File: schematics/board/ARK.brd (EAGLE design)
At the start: 89.6 x 89 mm, 207 parts, among them IC2 STM32F103C8T, Q5 8MHz

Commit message: Изменения в компоновке БКУ
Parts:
- removed R25, R26: 10k, resistor:R0603
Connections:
- removed net N$156: IC2.38, R25.2
- removed net N$157: IC2.39, R26.2
- net VDD: no longer R25.1, R26.1
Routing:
- net N$156: track 4.93 -> 0.00 mm
- net N$157: track 4.22 -> 0.00 mm
- net VDD: track 279.9 -> 279.4 mm
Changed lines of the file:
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@@
 <attribute name="VALUE" x="62.53" y="20.945" size="1.27" layer="27"/>
 </element>
-<element name="R25" library="resistor" library_urn="urn:adsk.eagle:library:348" package="R0603" package3d_urn="urn:adsk.eagle:package:23555/3" value="10k" x="61.1" y="25.78" smashed="yes" rot="R90"/>
-<element name="R26" library="resistor" library_urn="urn:adsk.eagle:library:348" package="R0603" package3d_urn="urn:adsk.eagle:package:23555/3" value="10k" x="63.3" y="25.78" smashed="yes" rot="R90"/>
 <element name="R27" library="resistor" library_urn="urn:adsk.eagle:library:348" package="R0603" package3d_urn="urn:adsk.eagle:package:23555/3" value="10k" x="58.9" y="25.78" smashed="yes" rot="R90"/>
 <element name="R64" library="resistor" library_urn="urn:adsk.eagle:library:348" package="R0603" package3d_urn="urn:adsk.eagle:package:23555/3" value="10k" x="56.7" y="25.78" smashed="yes" rot="R90"/>
@@
 <contactref element="AB2" pad="3"/>
 <contactref element="AB1" pad="3"/>
-<contactref element="R25" pad="1"/>
-<contactref element="R26" pad="1"/>
 <contactref element="R27" pad="1"/>
 <contactref element="R64" pad="1"/>
@@
 <wire x1="56.7" y1="24.93" x2="57.85" y2="24.93" width="0.3" layer="1"/>
 <wire x1="57.85" y1="24.93" x2="58.9" y2="24.93" width="0.3" layer="1"/>
-<wire x1="61.1" y1="24.93" x2="58.9" y2="24.93" width="0.3" layer="1"/>
-<wire x1="61.1" y1="24.93" x2="63.3" y2="24.93" width="0.3" layer="1"/>
-<wire x1="63.3" y1="24.93" x2="63.05" y2="24.68" width="0.3" layer="1"/>
-<wire x1="63.05" y1="24.68" x2="63.05" y2="22.85" width="0.3" layer="1"/>
+<wire x1="63.05" y1="22.85" x2="63.05" y2="24.68" width="0.3" layer="1"/>
 <wire x1="63.05" y1="22.85" x2="63.05" y2="22.1" width="0.3" layer="1"/>
 <wire x1="63.05" y1="22.1" x2="63.05" y2="21.3" width="0.3" layer="1"/>
@@
 <wire x1="61.75" y1="39.55" x2="62.27478125" y2="39.02521875" width="0.25" layer="1"/>
 <wire x1="62.27478125" y1="39.02521875" x2="62.5206375" y2="39.02521875" width="0.25" layer="1"/>
+<wire x1="63.05" y1="24.68" x2="62.8" y2="24.93" width="0.3" layer="1"/>
+<wire x1="62.8" y1="24.93" x2="58.9" y2="24.93" width="0.3" layer="1"/>
 </signal>
 <signal name="GND">
@@
 <wire x1="73.05" y1="27.8" x2="74.55" y2="27.8" width="0.3" layer="1"/>
 </signal>
-<signal name="N$156">
-<contactref element="R25" pad="2"/>
-<wire x1="61.1" y1="26.63" x2="63.05" y2="28.58" width="0.3" layer="1"/>
-<wire x1="63.05" y1="28.58" x2="63.05" y2="30.75" width="0.3" layer="1"/>
-<contactref element="IC2" pad="38"/>
-</signal>
-<signal name="N$157">
-<contactref element="R26" pad="2"/>
-<wire x1="63.3" y1="26.63" x2="63.55" y2="26.88" width="0.3" layer="1"/>
-<wire x1="63.55" y1="30.75" x2="63.55" y2="26.88" width="0.3" layer="1"/>
-<contactref element="IC2" pad="39"/>
-</signal>
 <signal name="N$159">

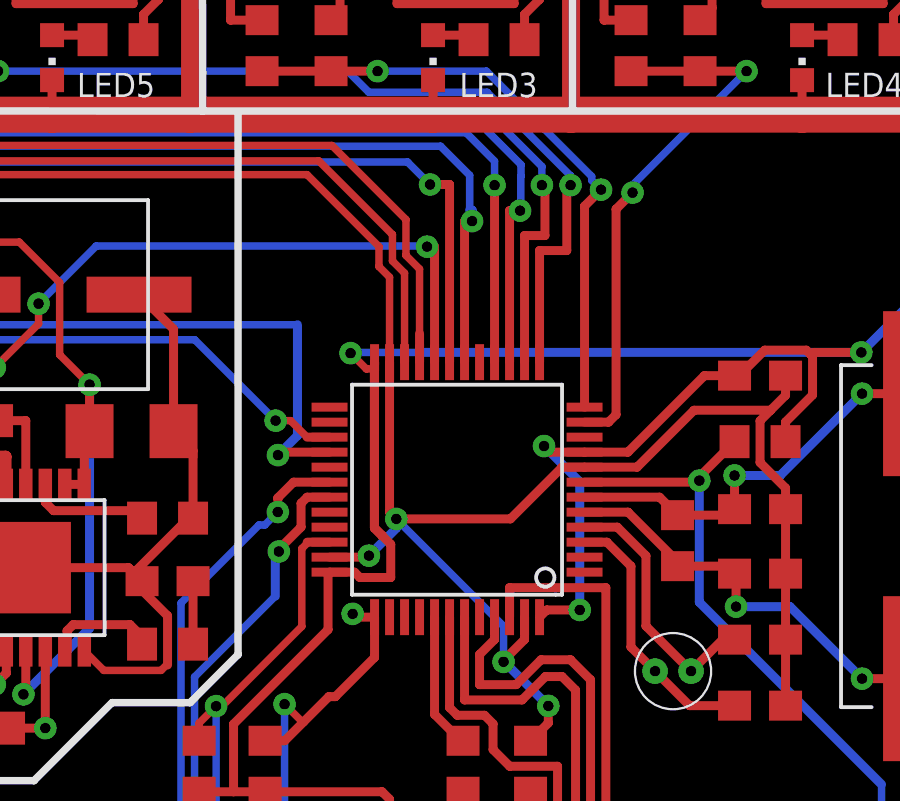
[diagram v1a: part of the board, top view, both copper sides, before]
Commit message: Исправлены АРК и БСК1
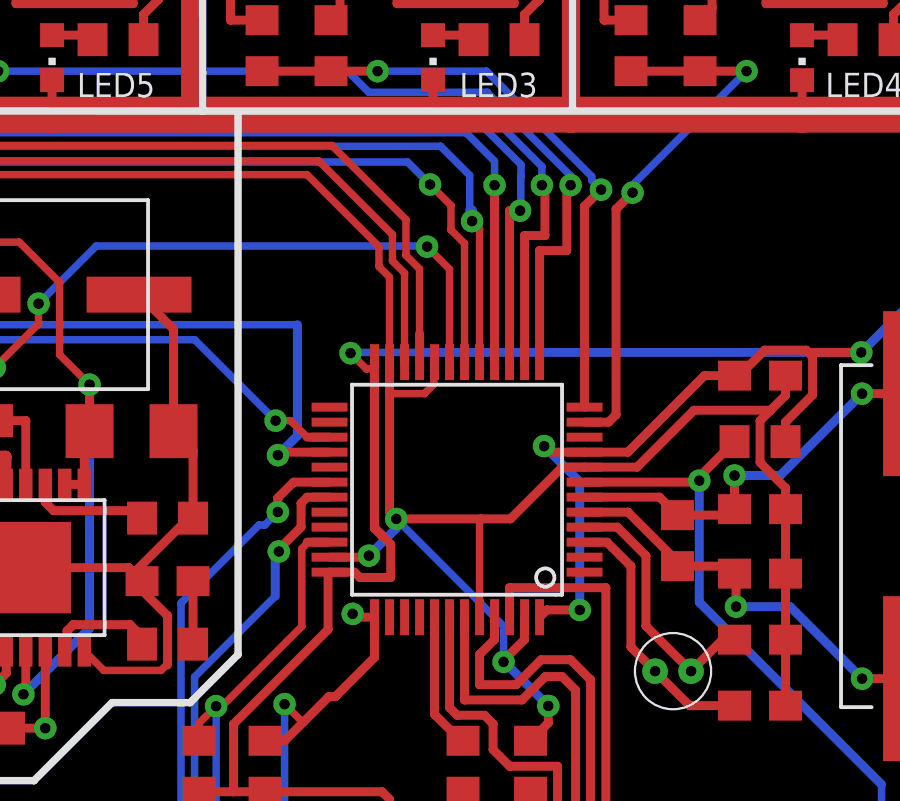
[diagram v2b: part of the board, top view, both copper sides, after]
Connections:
- net 1W: now also IC2.17; no longer IC2.18
- net GND: now also IC2.20, IC2.44
- net PGOOD1: now also IC2.18; no longer IC2.19
- net PGOOD2: now also IC2.19; no longer IC2.20
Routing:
- net GND: track 569.3 -> 574.9 mm
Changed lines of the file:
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@@
 <?xml version="1.0" encoding="utf-8"?>
 <!DOCTYPE eagle SYSTEM "eagle.dtd">
-<eagle version="9.6.0">
+<eagle version="9.4.2">
 <drawing>
 <settings>
@@
 <wire x1="63.05" y1="34.24983125" x2="63.274915625" y2="34.024915625" width="0.3" layer="1"/>
 <wire x1="69.55" y1="35.75" x2="68.805025" y2="35.75" width="0.3" layer="1"/>
-<wire x1="67.079940625" y1="34.024915625" x2="63.274915625" y2="34.024915625" width="0.3" layer="1"/>
+<wire x1="67.079940625" y1="34.024915625" x2="66.1" y2="34.024915625" width="0.3" layer="1"/>
+<wire x1="66.1" y1="34.024915625" x2="63.274915625" y2="34.024915625" width="0.3" layer="1"/>
 <wire x1="68.805025" y1="35.75" x2="67.079940625" y2="34.024915625" width="0.3" layer="1"/>
 <wire x1="51.55" y1="13.5" x2="52" y2="13.95" width="0.3" layer="1"/>
@@
 <wire x1="66.85" y1="29.26" x2="66.85" y2="29.305025" width="0.3" layer="1"/>
 <wire x1="66.85" y1="29.305025" x2="67.55" y2="30.005025" width="0.3" layer="1"/>
-<wire x1="63.05" y1="39.25" x2="63.05" y2="34.24983125" width="0.3" layer="1"/>
+<wire x1="63.05" y1="39.25" x2="63.05" y2="38.2" width="0.3" layer="1"/>
 <contactref element="R70" pad="1"/>
 <contactref element="R30" pad="2"/>
+<wire x1="63.05" y1="38.2" x2="63.05" y2="34.24983125" width="0.3" layer="1"/>
 <wire x1="46.4532" y1="36.35" x2="46.4532" y2="37.5968" width="0.3" layer="1"/>
 <wire x1="46.4532" y1="37.5968" x2="45.85" y2="38.2" width="0.3" layer="1"/>
@@
 <wire x1="63.274915625" y1="34.024915625" x2="66.85" y2="30.44983125" width="0.25" layer="16"/>
 <wire x1="66.85" y1="30.44983125" x2="66.85" y2="29.26" width="0.25" layer="16"/>
+<contactref element="IC2" pad="44"/>
+<contactref element="IC2" pad="20"/>
+<wire x1="64.55" y1="39.25" x2="64.525" y2="39.225" width="0.25" layer="1"/>
+<wire x1="64.525" y1="39.225" x2="64.525" y2="38.51538125" width="0.25" layer="1"/>
+<wire x1="64.525" y1="38.51538125" x2="64.20961875" y2="38.2" width="0.25" layer="1"/>
+<wire x1="64.20961875" y1="38.2" x2="63.05" y2="38.2" width="0.25" layer="1"/>
+<wire x1="66.05" y1="30.75" x2="66.05" y2="33.974915625" width="0.25" layer="1"/>
+<wire x1="66.05" y1="33.974915625" x2="66.1" y2="34.024915625" width="0.25" layer="1"/>
 </signal>
 <signal name="N$131">
@@
 <wire x1="20.72" y1="77.95" x2="20.72" y2="73.85" width="0.3" layer="16"/>
 <wire x1="20.72" y1="73.85" x2="20.77" y2="73.8" width="0.3" layer="16"/>
-<wire x1="65.55" y1="39.25" x2="65.55" y2="43.95" width="0.3" layer="1"/>
-<wire x1="65.55" y1="43.95" x2="65.8" y2="43.95" width="0.3" layer="1"/>
 <via x="65.8" y="43.95" extent="1-16" drill="0.35"/>
 <wire x1="65.8" y1="43.95" x2="65.8" y2="44.3202" width="0.3" layer="16"/>
@@
 <wire x1="12.8404" y1="47.1" x2="39.3702" y2="47.1" width="0.3" layer="16"/>
 <wire x1="11.8202" y1="49.7798" x2="39.45" y2="49.7798" width="0.3" layer="16"/>
-<contactref element="IC2" pad="18"/>
 <wire x1="39.3702" y1="47.1" x2="48.946325" y2="47.1" width="0.25" layer="16"/>
 <wire x1="48.946325" y1="47.1" x2="49.599525" y2="46.4468" width="0.25" layer="16"/>
@@
 <wire x1="65.7202" y1="45.4798" x2="65.7202" y2="44.3202" width="0.25" layer="16"/>
 <wire x1="64.7532" y1="46.4468" x2="65.7202" y2="45.4798" width="0.25" layer="16"/>
+<contactref element="IC2" pad="17"/>
+<wire x1="65.8" y1="43.95" x2="66.05" y2="43.7" width="0.25" layer="1"/>
+<wire x1="66.05" y1="43.7" x2="66.05" y2="39.25" width="0.25" layer="1"/>
 </signal>
 <signal name="N$147">
@@
 <via x="64.3" y="43.1" extent="1-16" drill="0.35"/>
 <wire x1="64.3" y1="43.1202" x2="64.3" y2="43.1" width="0.3" layer="16"/>
-<wire x1="64.3" y1="43.1" x2="64.55" y2="43.1" width="0.3" layer="1"/>
-<wire x1="64.55" y1="43.1" x2="64.55" y2="39.25" width="0.3" layer="1"/>
-<contactref element="IC2" pad="20"/>
 <wire x1="49.8904" y1="28.5" x2="49.8904" y2="39.0680625" width="0.25" layer="16"/>
 <via x="49.8904" y="39.0680625" extent="1-16" drill="0.35"/>
@@
 <wire x1="51.35" y1="41.2" x2="53.2702" y2="43.1202" width="0.25" layer="16"/>
 <wire x1="53.2702" y1="43.1202" x2="64.3" y2="43.1202" width="0.25" layer="16"/>
+<contactref element="IC2" pad="19"/>
+<wire x1="64.3" y1="43.1" x2="65.05" y2="42.35" width="0.25" layer="1"/>
+<wire x1="65.05" y1="42.35" x2="65.05" y2="39.25" width="0.25" layer="1"/>
 </signal>
 <signal name="N$129">
@@
 <wire x1="12.9596" y1="37.03440625" x2="12.8696" y2="37.12440625" width="0.3" layer="16"/>
 <via x="64.4" y="45.1718" extent="1-16" drill="0.35"/>
-<wire x1="64.4" y1="45.1718" x2="65.05" y2="45.1718" width="0.3" layer="1"/>
-<wire x1="65.05" y1="45.1718" x2="65.05" y2="39.25" width="0.3" layer="1"/>
-<contactref element="IC2" pad="19"/>
 <wire x1="12.87315625" y1="43.50355625" x2="12.8696" y2="43.5" width="0.3" layer="16"/>
 <wire x1="24.95675625" y1="45.0532" x2="23.4071125" y2="43.50355625" width="0.3" layer="16"/>
@@
 <wire x1="63.65" y1="45.9218" x2="64.4" y2="45.1718" width="0.25" layer="16"/>
 <wire x1="63.65" y1="45.9218" x2="38.1654" y2="45.9218" width="0.25" layer="16"/>
+<contactref element="IC2" pad="18"/>
+<wire x1="64.4" y1="45.1718" x2="65.0968" y2="44.475" width="0.25" layer="1"/>
+<wire x1="65.55" y1="43.205525" x2="65.55" y2="39.25" width="0.25" layer="1"/>
+<wire x1="65.0968" y1="44.475" x2="65.0968" y2="43.658725" width="0.25" layer="1"/>
+<wire x1="65.0968" y1="43.658725" x2="65.55" y2="43.205525" width="0.25" layer="1"/>
 </signal>
 <signal name="SWC">

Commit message: Добавлены подтяжки i2c
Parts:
- added R25, R26: 5k1, resistor:R0603
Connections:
- net SCLTM: now also R25.2
- net SDATM: now also R26.2
- net VDD: now also R25.1, R26.1
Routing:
- net VDD: track 279.4 -> 293.2 mm, vias 15 -> 16
- net SCLTM: track 49.3 -> 52.1 mm
- net SDATM: track 54.4 -> 56.3 mm, vias 0 -> 2
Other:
- board text added: "SCLTM"
- board text added: "SDATM"

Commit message: Резисторы у FS8205A 100Ом
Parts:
- R88, R89, R90, R91, R92, R93, R94, R95, R96, R97, R98, R99: value 10k -> 100R
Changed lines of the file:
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@@
 <element name="R62" library="resistor" library_urn="urn:adsk.eagle:library:348" package="R0603" package3d_urn="urn:adsk.eagle:package:23555/3" value="232k" x="12.7" y="16.85" smashed="yes"/>
 <element name="R87" library="resistor" library_urn="urn:adsk.eagle:library:348" package="R0603" package3d_urn="urn:adsk.eagle:package:23555/3" value="680k" x="12.7" y="19" smashed="yes" rot="R180"/>
-<element name="R88" library="resistor" library_urn="urn:adsk.eagle:library:348" package="R0603" package3d_urn="urn:adsk.eagle:package:23555/3" value="10k" x="58.8" y="49.8" smashed="yes" rot="R90"/>
-<element name="R89" library="resistor" library_urn="urn:adsk.eagle:library:348" package="R0603" package3d_urn="urn:adsk.eagle:package:23555/3" value="10k" x="61.1" y="49.8" smashed="yes" rot="R90"/>
-<element name="R90" library="resistor" library_urn="urn:adsk.eagle:library:348" package="R0603" package3d_urn="urn:adsk.eagle:package:23555/3" value="10k" x="71.1" y="49.8" smashed="yes" rot="R90"/>
-<element name="R91" library="resistor" library_urn="urn:adsk.eagle:library:348" package="R0603" package3d_urn="urn:adsk.eagle:package:23555/3" value="10k" x="73.4" y="49.8" smashed="yes" rot="R90"/>
-<element name="R92" library="resistor" library_urn="urn:adsk.eagle:library:348" package="R0603" package3d_urn="urn:adsk.eagle:package:23555/3" value="10k" x="46.1" y="49.8" smashed="yes" rot="R90"/>
-<element name="R93" library="resistor" library_urn="urn:adsk.eagle:library:348" package="R0603" package3d_urn="urn:adsk.eagle:package:23555/3" value="10k" x="48.4" y="49.8" smashed="yes" rot="R90"/>
-<element name="R94" library="resistor" library_urn="urn:adsk.eagle:library:348" package="R0603" package3d_urn="urn:adsk.eagle:package:23555/3" value="10k" x="21.1" y="49.8" smashed="yes" rot="R90"/>
-<element name="R95" library="resistor" library_urn="urn:adsk.eagle:library:348" package="R0603" package3d_urn="urn:adsk.eagle:package:23555/3" value="10k" x="23.4" y="49.8" smashed="yes" rot="R90"/>
-<element name="R96" library="resistor" library_urn="urn:adsk.eagle:library:348" package="R0603" package3d_urn="urn:adsk.eagle:package:23555/3" value="10k" x="33.8" y="49.8" smashed="yes" rot="R90"/>
-<element name="R97" library="resistor" library_urn="urn:adsk.eagle:library:348" package="R0603" package3d_urn="urn:adsk.eagle:package:23555/3" value="10k" x="36.1" y="49.8" smashed="yes" rot="R90"/>
-<element name="R98" library="resistor" library_urn="urn:adsk.eagle:library:348" package="R0603" package3d_urn="urn:adsk.eagle:package:23555/3" value="10k" x="8.8" y="49.8" smashed="yes" rot="R90"/>
-<element name="R99" library="resistor" library_urn="urn:adsk.eagle:library:348" package="R0603" package3d_urn="urn:adsk.eagle:package:23555/3" value="10k" x="11.1" y="49.8" smashed="yes" rot="R90"/>
+<element name="R88" library="resistor" library_urn="urn:adsk.eagle:library:348" package="R0603" package3d_urn="urn:adsk.eagle:package:23555/3" value="100R" x="58.8" y="49.8" smashed="yes" rot="R90"/>
+<element name="R89" library="resistor" library_urn="urn:adsk.eagle:library:348" package="R0603" package3d_urn="urn:adsk.eagle:package:23555/3" value="100R" x="61.1" y="49.8" smashed="yes" rot="R90"/>
+<element name="R90" library="resistor" library_urn="urn:adsk.eagle:library:348" package="R0603" package3d_urn="urn:adsk.eagle:package:23555/3" value="100R" x="71.1" y="49.8" smashed="yes" rot="R90"/>
+<element name="R91" library="resistor" library_urn="urn:adsk.eagle:library:348" package="R0603" package3d_urn="urn:adsk.eagle:package:23555/3" value="100R" x="73.4" y="49.8" smashed="yes" rot="R90"/>
+<element name="R92" library="resistor" library_urn="urn:adsk.eagle:library:348" package="R0603" package3d_urn="urn:adsk.eagle:package:23555/3" value="100R" x="46.1" y="49.8" smashed="yes" rot="R90"/>
+<element name="R93" library="resistor" library_urn="urn:adsk.eagle:library:348" package="R0603" package3d_urn="urn:adsk.eagle:package:23555/3" value="100R" x="48.4" y="49.8" smashed="yes" rot="R90"/>
+<element name="R94" library="resistor" library_urn="urn:adsk.eagle:library:348" package="R0603" package3d_urn="urn:adsk.eagle:package:23555/3" value="100R" x="21.1" y="49.8" smashed="yes" rot="R90"/>
+<element name="R95" library="resistor" library_urn="urn:adsk.eagle:library:348" package="R0603" package3d_urn="urn:adsk.eagle:package:23555/3" value="100R" x="23.4" y="49.8" smashed="yes" rot="R90"/>
+<element name="R96" library="resistor" library_urn="urn:adsk.eagle:library:348" package="R0603" package3d_urn="urn:adsk.eagle:package:23555/3" value="100R" x="33.8" y="49.8" smashed="yes" rot="R90"/>
+<element name="R97" library="resistor" library_urn="urn:adsk.eagle:library:348" package="R0603" package3d_urn="urn:adsk.eagle:package:23555/3" value="100R" x="36.1" y="49.8" smashed="yes" rot="R90"/>
+<element name="R98" library="resistor" library_urn="urn:adsk.eagle:library:348" package="R0603" package3d_urn="urn:adsk.eagle:package:23555/3" value="100R" x="8.8" y="49.8" smashed="yes" rot="R90"/>
+<element name="R99" library="resistor" library_urn="urn:adsk.eagle:library:348" package="R0603" package3d_urn="urn:adsk.eagle:package:23555/3" value="100R" x="11.1" y="49.8" smashed="yes" rot="R90"/>
 <element name="PWR" library="led" library_urn="urn:adsk.eagle:library:259" package="CHIPLED_0603" package3d_urn="urn:adsk.eagle:package:15822/2" value="" x="63.8" y="21.3" smashed="yes" rot="R270">
 <attribute name="NAME" x="59.78" y="20.935" size="0.8128" layer="25"/>

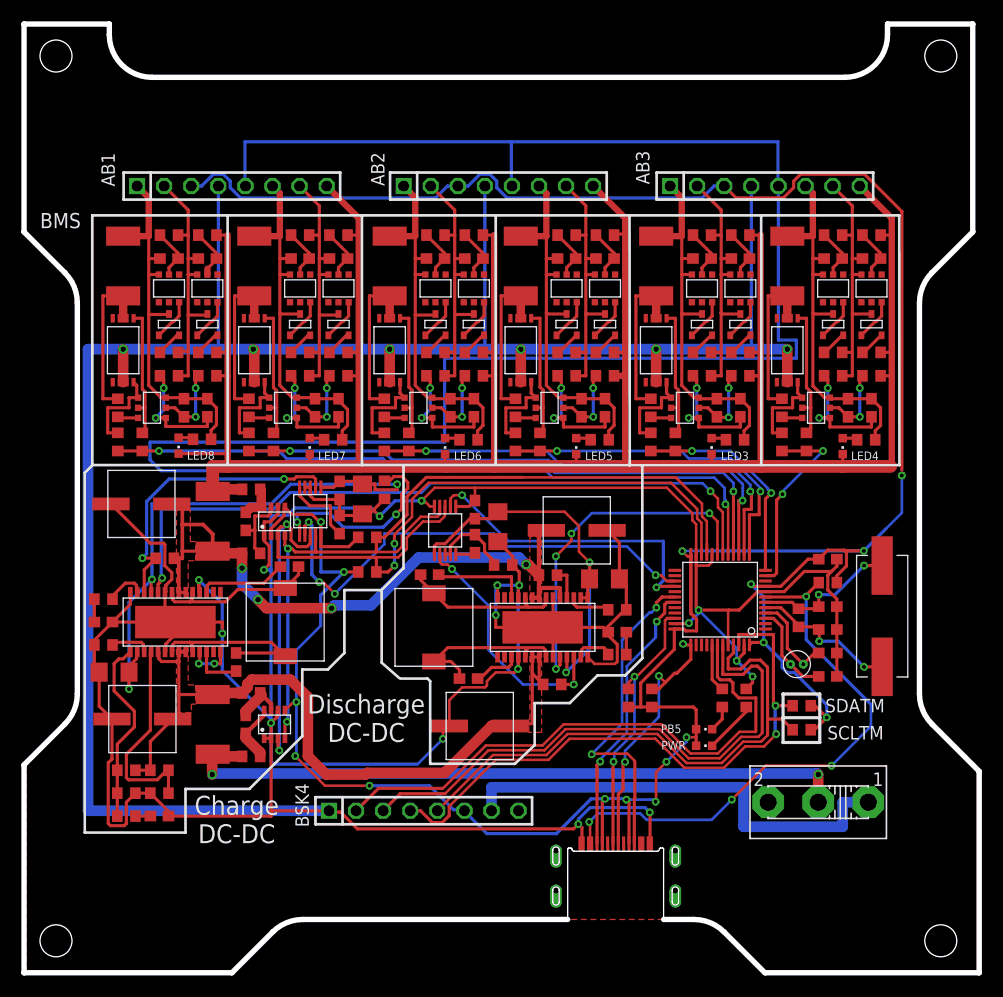
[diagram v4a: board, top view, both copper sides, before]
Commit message: Добавлен micro-USB на АРК
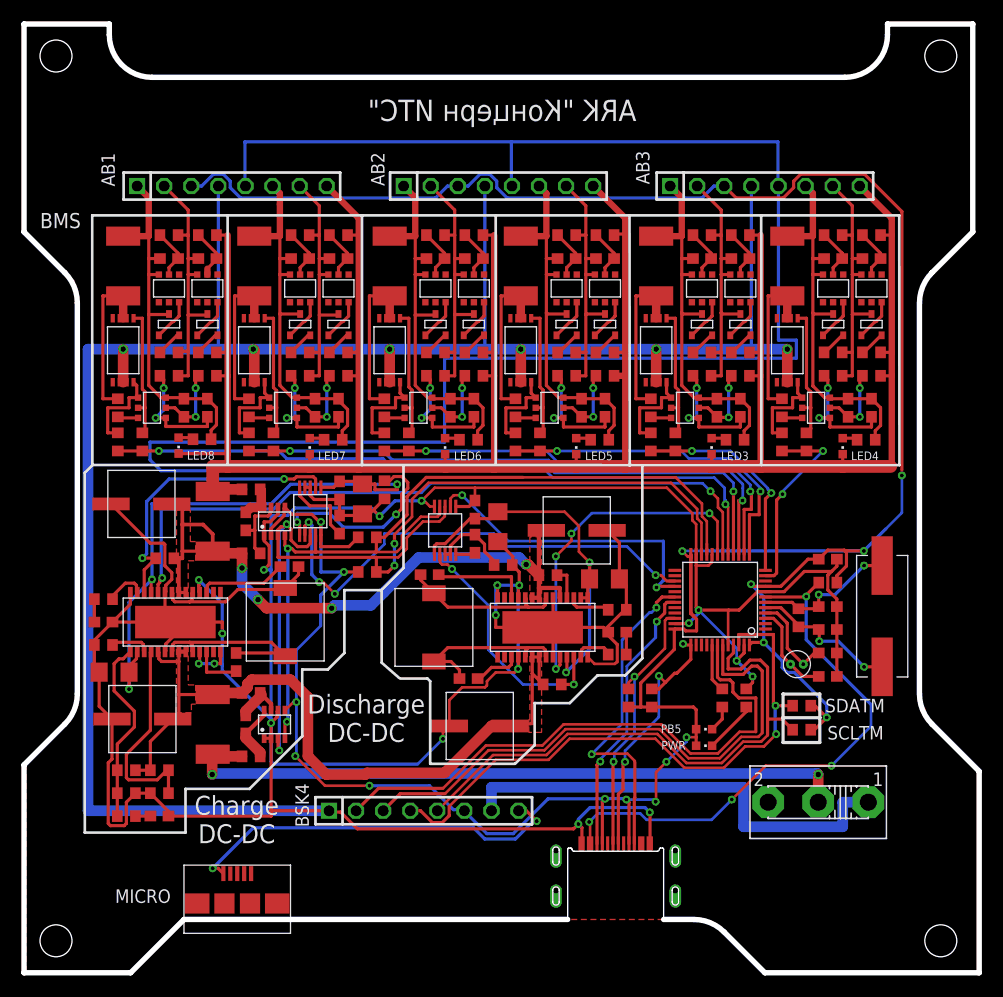
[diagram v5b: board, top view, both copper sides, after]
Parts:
- added MICRO: 629105136821, MicroUSB:629105136821
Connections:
- net 5V: now also MICRO.5V
- net GND: now also MICRO.GND, MICRO.Z1, MICRO.Z2, MICRO.Z3, MICRO.Z4
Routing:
- net 5V: track 0.00 -> 36.4 mm, vias 0 -> 2
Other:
- outline, holes or cut-outs redrawn
